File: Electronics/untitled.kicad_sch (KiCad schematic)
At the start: 28 parts, among them J13 4DB-P108-03

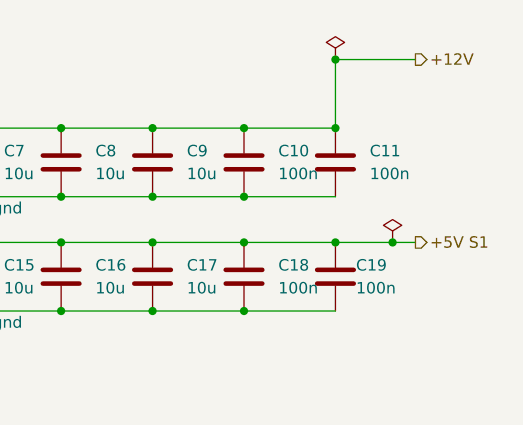
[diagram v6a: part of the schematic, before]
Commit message: More pcb arangment, verticle ports
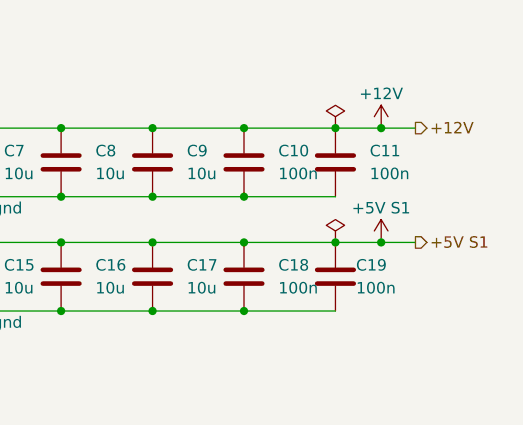
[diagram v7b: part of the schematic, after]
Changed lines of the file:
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@@
 	)
 	(junction
+		(at 167.64 53.34)
+		(diameter 0)
+		(color 0 0 0 0)
+	)
+	(junction
 		(at 101.6 40.64)
 		(diameter 0)
@@
 	)
 	(junction
-		(at 162.56 33.02)
-		(diameter 0)
-		(color 0 0 0 0)
-	)
-	(junction
 		(at 78.74 53.34)
 		(diameter 0)
@@
 	)
 	(junction
-		(at 168.91 53.34)
+		(at 167.64 40.64)
 		(diameter 0)
 		(color 0 0 0 0)
@@
 	(wire
 		(pts
-			(xy 168.91 53.34) (xy 171.45 53.34)
-		)
-		(stroke
-			(width 0)
-			(type default)
-		)
-	)
-	(wire
-		(pts
 			(xy 95.25 68.58) (xy 96.52 68.58)
 		)
@@
 	(wire
 		(pts
-			(xy 162.56 33.02) (xy 171.45 33.02)
-		)
-		(stroke
-			(width 0)
-			(type default)
-		)
-	)
-	(wire
-		(pts
 			(xy 142.24 53.34) (xy 132.08 53.34)
 		)
@@
 	(wire
 		(pts
-			(xy 162.56 53.34) (xy 168.91 53.34)
+			(xy 167.64 53.34) (xy 171.45 53.34)
 		)
 		(stroke
@@
 	(wire
 		(pts
-			(xy 162.56 40.64) (xy 162.56 33.02)
+			(xy 162.56 53.34) (xy 167.64 53.34)
 		)
 		(stroke
@@
 	(wire
 		(pts
+			(xy 162.56 40.64) (xy 167.64 40.64)
+		)
+		(stroke
+			(width 0)
+			(type default)
+		)
+	)
+	(wire
+		(pts
 			(xy 142.24 60.96) (xy 152.4 60.96)
 		)
@@
 	(wire
 		(pts
+			(xy 167.64 40.64) (xy 171.45 40.64)
+		)
+		(stroke
+			(width 0)
+			(type default)
+		)
+	)
+	(wire
+		(pts
 			(xy 78.74 68.58) (xy 78.74 60.96)
 		)
@@
 	(hierarchical_label "+12V"
 		(shape output)
-		(at 171.45 33.02 0)
+		(at 171.45 40.64 0)
 		(effects
 			(font
@@
 		(dnp no)
 		(fields_autoplaced yes)
-		(property "Reference" "#PWR026"
+		(property "Reference" "#PWR028"
 			(at 31.75 64.77 0)
 			(effects
@@
 			(project "CM5 Nas"
 				(path "/0650c7a8-acba-429c-9f8e-eec0baf0bc1c/fede4c36-00cc-4d3d-b71c-5243ba232202/ff10faca-55ce-4526-b63b-58be6b3f0345"
-					(reference "#PWR026")
+					(reference "#PWR028")
 					(unit 1)
 				)
@@
 	(symbol
 		(lib_id "power:PWR_FLAG")
-		(at 162.56 33.02 0)
+		(at 162.56 40.64 0)
 		(unit 1)
 		(exclude_from_sim no)
@@
 		(fields_autoplaced yes)
 		(property "Reference" "#FLG01"
-			(at 162.56 31.115 0)
+			(at 162.56 38.735 0)
 			(effects
 				(font
@@
 		)
 		(property "Value" "PWR_FLAG"
-			(at 162.56 27.94 0)
+			(at 162.56 35.56 0)
 			(effects
 				(font
@@
 		)
 		(property "Footprint" ""
-			(at 162.56 33.02 0)
+			(at 162.56 40.64 0)
 			(effects
 				(font
@@
 		)
 		(property "Datasheet" "~"
-			(at 162.56 33.02 0)
+			(at 162.56 40.64 0)
 			(effects
 				(font
@@
 		)
 		(property "Description" "Special symbol for telling ERC where power comes from"
-			(at 162.56 33.02 0)
+			(at 162.56 40.64 0)
 			(effects
 				(font
@@
 		(dnp no)
 		(fields_autoplaced yes)
-		(property "Reference" "#PWR027"
+		(property "Reference" "#PWR029"
 			(at 121.92 67.31 0)
 			(effects
@@
 			(project "CM5 Nas"
 				(path "/0650c7a8-acba-429c-9f8e-eec0baf0bc1c/fede4c36-00cc-4d3d-b71c-5243ba232202/ff10faca-55ce-4526-b63b-58be6b3f0345"
-					(reference "#PWR027")
+					(reference "#PWR029")
 					(unit 1)
 				)
@@
 		(dnp no)
 		(fields_autoplaced yes)
-		(property "Reference" "#PWR028"
+		(property "Reference" "#PWR030"
 			(at 105.41 76.2 0)
 			(effects
@@
 			(project "CM5 Nas"
 				(path "/0650c7a8-acba-429c-9f8e-eec0baf0bc1c/fede4c36-00cc-4d3d-b71c-5243ba232202/ff10faca-55ce-4526-b63b-58be6b3f0345"
-					(reference "#PWR028")
+					(reference "#PWR030")
 					(unit 1)
 				)
@@
 		(dnp no)
 		(fields_autoplaced yes)
-		(property "Reference" "#PWR025"
+		(property "Reference" "#PWR026"
 			(at 121.92 54.61 0)
 			(effects
@@
 			(project "CM5 Nas"
 				(path "/0650c7a8-acba-429c-9f8e-eec0baf0bc1c/fede4c36-00cc-4d3d-b71c-5243ba232202/ff10faca-55ce-4526-b63b-58be6b3f0345"
-					(reference "#PWR025")
+					(reference "#PWR026")
 					(unit 1)
 				)
@@
 	)
 	(symbol
+		(lib_id "power:+5V")
+		(at 167.64 53.34 0)
+		(unit 1)
+		(exclude_from_sim no)
+		(in_bom yes)
+		(on_board yes)
+		(dnp no)
+		(property "Reference" "#PWR027"
+			(at 167.64 57.15 0)
+			(effects
+				(font
+					(size 1.27 1.27)
+				)
+				(hide yes)
+			)
+		)
+		(property "Value" "+5V S1"
+			(at 167.64 49.53 0)
+			(effects
+				(font
+					(size 1.27 1.27)
+				)
+			)
+		)
+		(property "Footprint" ""
+			(at 167.64 53.34 0)
+			(effects
+				(font
+					(size 1.27 1.27)
+				)
+				(hide yes)
+			)
+		)
+		(property "Datasheet" ""
+			(at 167.64 53.34 0)
+			(effects
+				(font
+					(size 1.27 1.27)
+				)
+				(hide yes)
+			)
+		)
+		(property "Description" "Power symbol creates a global label with name \"+5V\""
+			(at 167.64 53.34 0)
+			(effects
+				(font
+					(size 1.27 1.27)
+				)
+				(hide yes)
+			)
+		)
+		(pin "1"
+		)
+		(instances
+			(project ""
+				(path "/0650c7a8-acba-429c-9f8e-eec0baf0bc1c/fede4c36-00cc-4d3d-b71c-5243ba232202/ff10faca-55ce-4526-b63b-58be6b3f0345"
+					(reference "#PWR027")
+					(unit 1)
+				)
+			)
+		)
+	)
+	(symbol
 		(lib_id "Device:C")
 		(at 132.08 44.45 0)
@@
 	(symbol
 		(lib_id "power:PWR_FLAG")
-		(at 168.91 53.34 0)
+		(at 162.56 53.34 0)
 		(unit 1)
 		(exclude_from_sim no)
@@
 		(fields_autoplaced yes)
 		(property "Reference" "#FLG02"
-			(at 168.91 51.435 0)
+			(at 162.56 51.435 0)
 			(effects
 				(font
@@
 		)
 		(property "Value" "PWR_FLAG"
-			(at 168.91 48.26 0)
+			(at 162.56 48.26 0)
 			(effects
 				(font
@@
 		)
 		(property "Footprint" ""
-			(at 168.91 53.34 0)
+			(at 162.56 53.34 0)
 			(effects
 				(font
@@
 		)
 		(property "Datasheet" "~"
-			(at 168.91 53.34 0)
+			(at 162.56 53.34 0)
 			(effects
 				(font
@@
 		)
 		(property "Description" "Special symbol for telling ERC where power comes from"
-			(at 168.91 53.34 0)
+			(at 162.56 53.34 0)
 			(effects
 				(font
@@
 					(unit 1)
 				)
+			)
+		)
+	)
+	(symbol
+		(lib_id "power:+12V")
+		(at 167.64 40.64 0)
+		(unit 1)
+		(exclude_from_sim no)
+		(in_bom yes)
+		(on_board yes)
+		(dnp no)
+		(property "Reference" "#PWR025"
+			(at 167.64 44.45 0)
+			(effects
+				(font
+					(size 1.27 1.27)
+				)
+				(hide yes)
+			)
+		)
+		(property "Value" "+12V"
+			(at 167.64 36.83 0)
+			(effects
+				(font
+					(size 1.27 1.27)
+				)
+			)
+		)
+		(property "Footprint" ""
+			(at 167.64 40.64 0)
+			(effects
+				(font
+					(size 1.27 1.27)
+				)
+				(hide yes)
+			)
+		)
+		(property "Datasheet" ""
+			(at 167.64 40.64 0)
+			(effects
+				(font
+					(size 1.27 1.27)
+				)
+				(hide yes)
+			)
+		)
+		(property "Description" "Power symbol creates a global label with name \"+12V\""
+			(at 167.64 40.64 0)
+			(effects
+				(font
+					(size 1.27 1.27)
+				)
+				(hide yes)
+			)
+		)
+		(pin "1"
+		)
+		(instances
+			(project ""
+				(path "/0650c7a8-acba-429c-9f8e-eec0baf0bc1c/fede4c36-00cc-4d3d-b71c-5243ba232202/ff10faca-55ce-4526-b63b-58be6b3f0345"
+					(reference "#PWR025")
+					(unit 1)
+				)
